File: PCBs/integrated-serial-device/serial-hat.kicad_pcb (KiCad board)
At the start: 2 copper layers, 193 x 113 mm, 28 parts, among them CN1 Modem port, CN2 Modem out 3, CN3 Printer port, J1 Rpi headers, J3 Conn_01x02_Pin, K1 Quicktake, K2 ImageWriter, SW1 Modem To Proxy, SW2 Modem to Quicktake, SW3 Modem out 3, SW5 Printer to Proxy, SW6 Printer to ImageWriter, SW7 SW_SPST, SW8 SW_Slide_DPDT SHOU HAN MSK-22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, U1 MAX3232

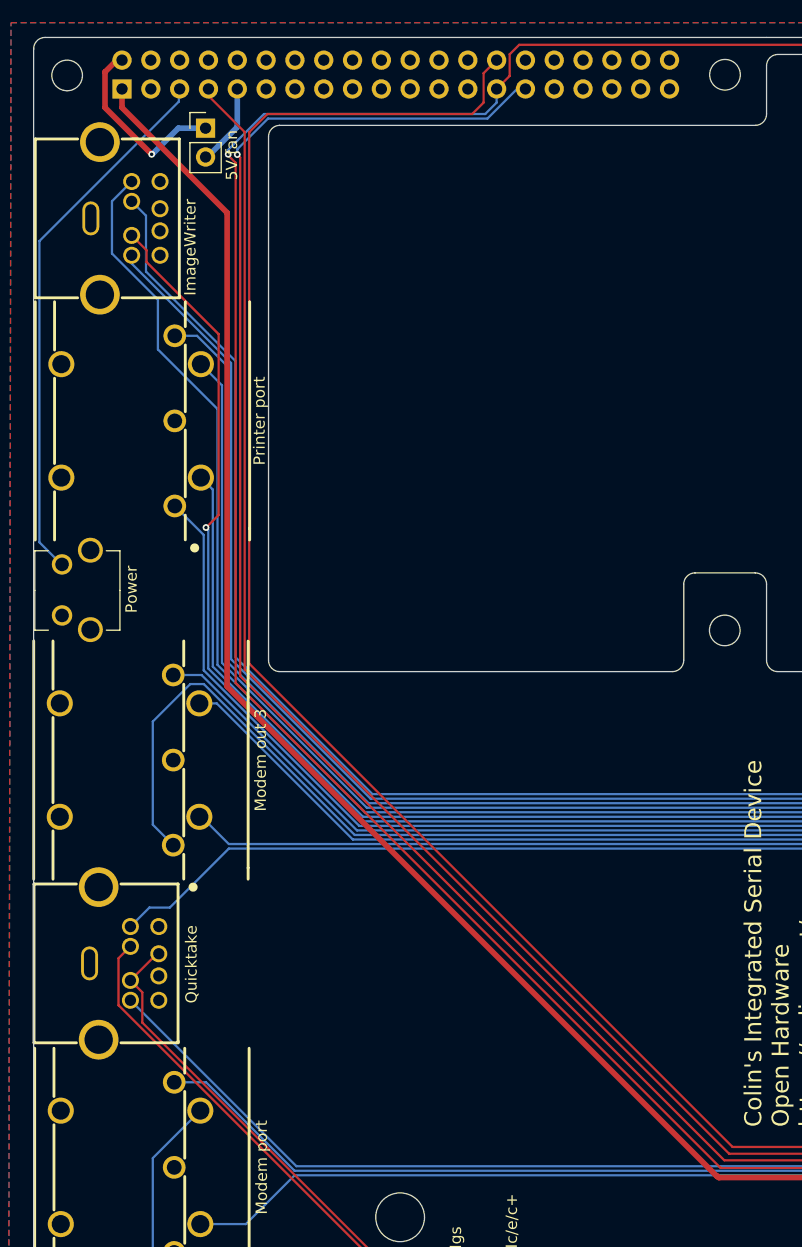
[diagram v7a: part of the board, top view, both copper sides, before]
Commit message: Add gpio-fan ability
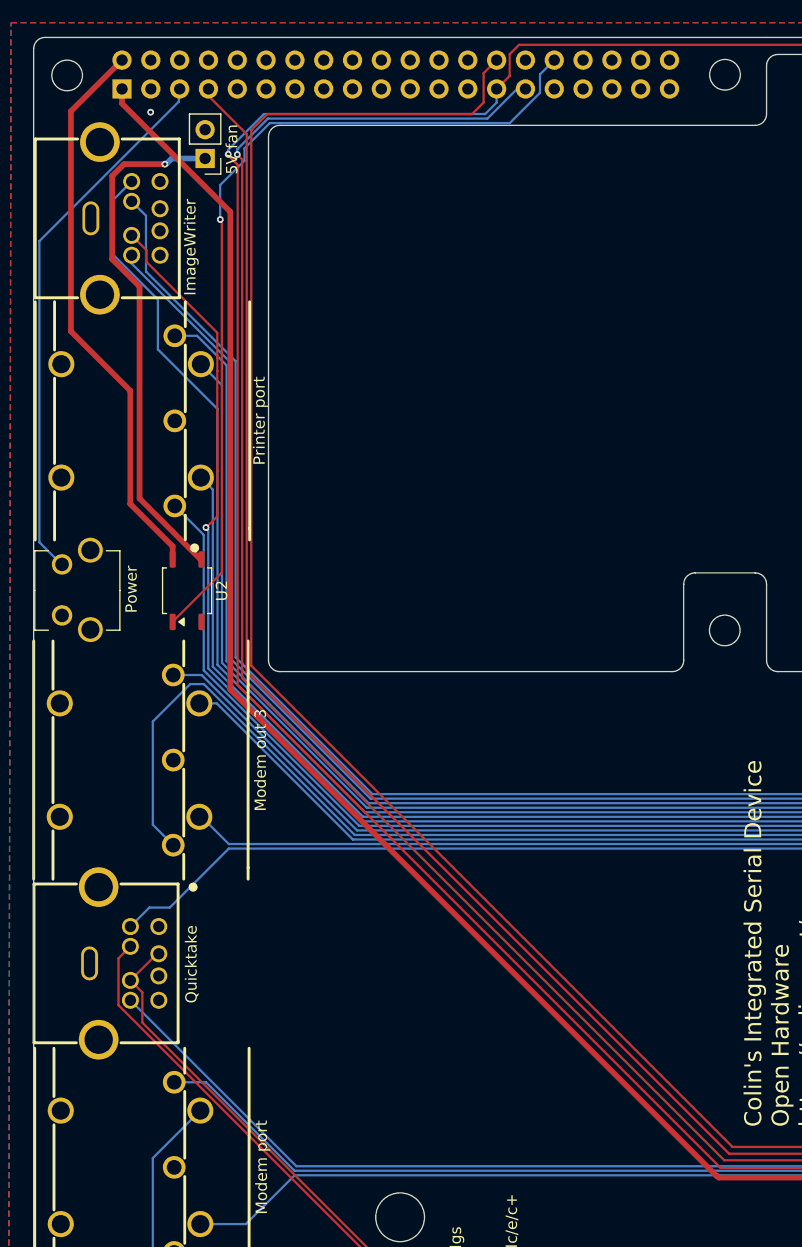
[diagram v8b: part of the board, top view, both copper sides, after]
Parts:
- added U2: PC817C-S, Package_SO:SOP-4_3.8x4.1mm_P2.54mm, F.Cu at (67.3, 87.5)
- moved J3 2.67 mm to (68.9, 49.4), turned to 180 degrees
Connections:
- J1 pad 32: unconnected-(J1-Pin_32-Pad32) -> FAN_CTRL
- J3 pad 1: 5V -> FAN_5V
- K2 pad 8: unconnected-(K2-Pad8) -> GND
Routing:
- net FAN_CTRL: track 0.00 -> 76.0 mm, vias 0 -> 1
- net FAN_5V: track 0.00 -> 45.9 mm, vias 0 -> 1
- net 5V: track 16.6 -> 49.6 mm, vias 1 -> 0
- net GND: track 16.6 -> 9.35 mm, vias 0 -> 1
